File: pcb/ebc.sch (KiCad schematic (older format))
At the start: 43 parts, among them P1 HE10-10, SW1 Switch_SPDT_x2, SW10 SW_PUSH, SW2 SW_PUSH, SW3 SW_PUSH, SW4 SW_PUSH, SW5 SW_PUSH, SW6 SW_PUSH, SW7 SW_PUSH, SW8 SW_PUSH, SW9 SW_PUSH, U1 M24SR64-Y, U2 MSP432P401R, X1 XC9142

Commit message: - schematic almost finished. just trying to pass electrical check
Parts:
- added C15, C18, C19: 10u, symbol C_Small
- added C16, C17: 1u, symbol C_Small
- added D3, D4: RED, symbol LED
- added D5, D6: 1N4148, symbol D_Small
- added P2: CONN_01X30, symbol CONN_01X30
- added R10, R9: 68, symbol R
- added R11: 50, symbol R_Small
- added R12: 600k, symbol R_Small
- D1: value LED -> RED
- gave numbers to parts that had none: 10
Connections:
- net +3V3: now also C18.1, C19.1, P2.17 (P17), P2.18 (P18), P2.27 (P27), P2.4 (P4)
- net 13V: now also C15.1, P2.2 (P2)
- net GND: now also C15.2, C16.2, C17.2, C18.2, C19.2, D5.1 (K), P2.1 (P1), P2.28 (P28), P2.30 (P30), R10.1, R12.2, R9.1
- net ~SHDN: now also U2.6 (P1.2/UCA0RXD/UCA0SOM)
- net at U1.2 (AC0): now also U1.3 (AC1)
- net at X1.2 (GND): now also BT1.1, C2.1, L1.1, X1.3 (BAT)
- net D0: now reaches U2.32 (P3.0/PM_UCA2STE)
- net D0: now also P2.14 (P14)
- net D1: now reaches U2.33 (P3.1/PM_UCA2CLK)
- net D1: now also P2.13 (P13)
- net D2: now reaches U2.34 (P3.2/PM_UCA2RXD/PM_UCA2SOMI)
- net D2: now also P2.12 (P12)
- net D3: now reaches U2.35 (P3.3/PM_UCA2TXD/PM_UCA2SIMO)
- net D3: now also P2.11 (P11)
- net D4: now reaches U2.36 (P3.4/PM_UCB2STE)
- net D4: now also P2.10 (P10)
- net D5: now reaches U2.37 (P3.5/PM_UCB2CLK)
- net D5: now also P2.9 (P9)
- net D6: now reaches U2.38 (P3.6/PM_UCB2SIMO/PM_UCB2SDA)
- net D6: now also P2.8 (P8)
- net D7: now reaches U2.39 (P3.7/PM_UCB2SOMI/PM_UCB2SCL)
- net D7: now also P2.7 (P7)
- net STATUS1: now reaches U2.4 (P1.0/UCA0STE)
- net STATUS1: now also D3.2 (A)
- net CS#: now reaches U2.46 (P8.2/TA3.2/A23)
- net CS#: now also P2.19 (P19)
- net D/C#: now reaches U2.47 (P8.3/TA3CLK/A22)
- net D/C#: now also P2.20 (P20)
- net RES#: now reaches U2.48 (P8.4/A21)
- net RES#: now also P2.21 (P21)
- net E/RD#: now reaches U2.49 (P8.5/A20)
- net E/RD#: now also P2.15 (P15)
- net STATUS2: now reaches U2.5 (P1.1/UCA0CL)
- net STATUS2: now also D4.2 (A)
- net R/W#: now reaches U2.50 (P8.6/A19)
- net R/W#: now also P2.16 (P16)
- net SWCLKTCK renamed TCK
- net SWDIOTMS renamed TMS
- new net: P2.22 (P22), R12.1
- new net: C17.1, P2.26 (P26)
- new net: C16.1, P2.3 (P3)
- new net: P2.5 (P5), R11.1
- new net: D5.2 (A), D6.1 (K)
- new net: D6.2 (A), R11.2
- new net: D3.1 (K), R9.2
- new net: D4.1 (K), R10.2
- no-connect marks 1 -> 60
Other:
- note added: "88.9mm x 50.8\n3.5in x 2in"
- note added: "NC(GND)\nVCC\nVCOMH\nVDDIO\nVSL\nNC\nD7\nD6\nD5\nD4\nD3\nD2\nD1/SDIN\nD0/SCK\nE/RD#\nR/W#\nBS0\nBS1\nCS#\nD/C#\nRES#\nIREF\nGPIO1\nGPIO0\nNC\nVDD\nVCI\nVSS\nNC\nNC(GND)"
- note added: "Rref=(VCC-6V)/IREF\nRref=(13-6)/12.5u\nRref=600k"
- moved on the sheet: C10, C12, C13, C14, D2, L2, R3, R7, R8, SW10, SW2, SW3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

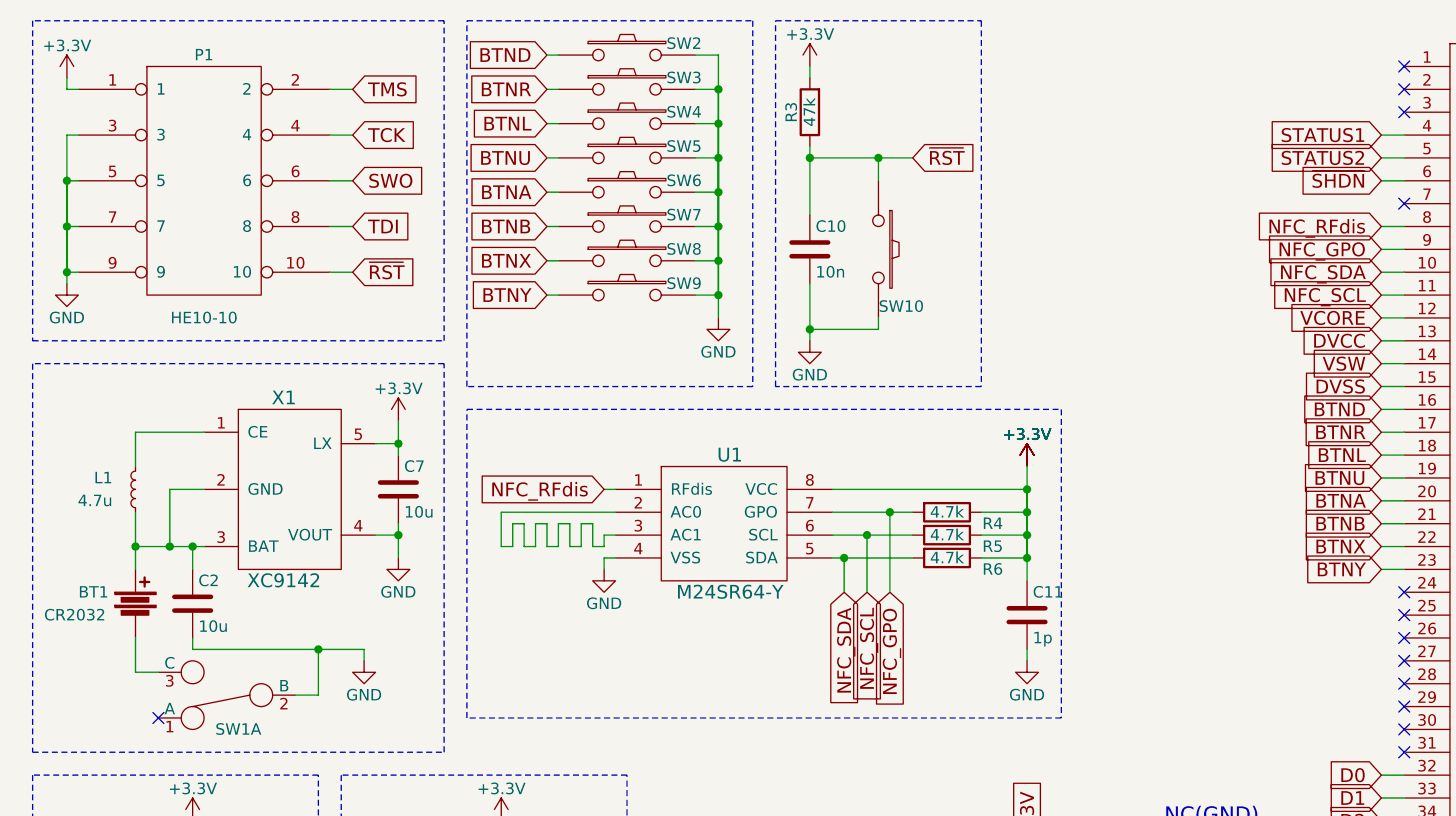
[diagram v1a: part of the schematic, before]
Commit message: - netlist generated, component selection begun
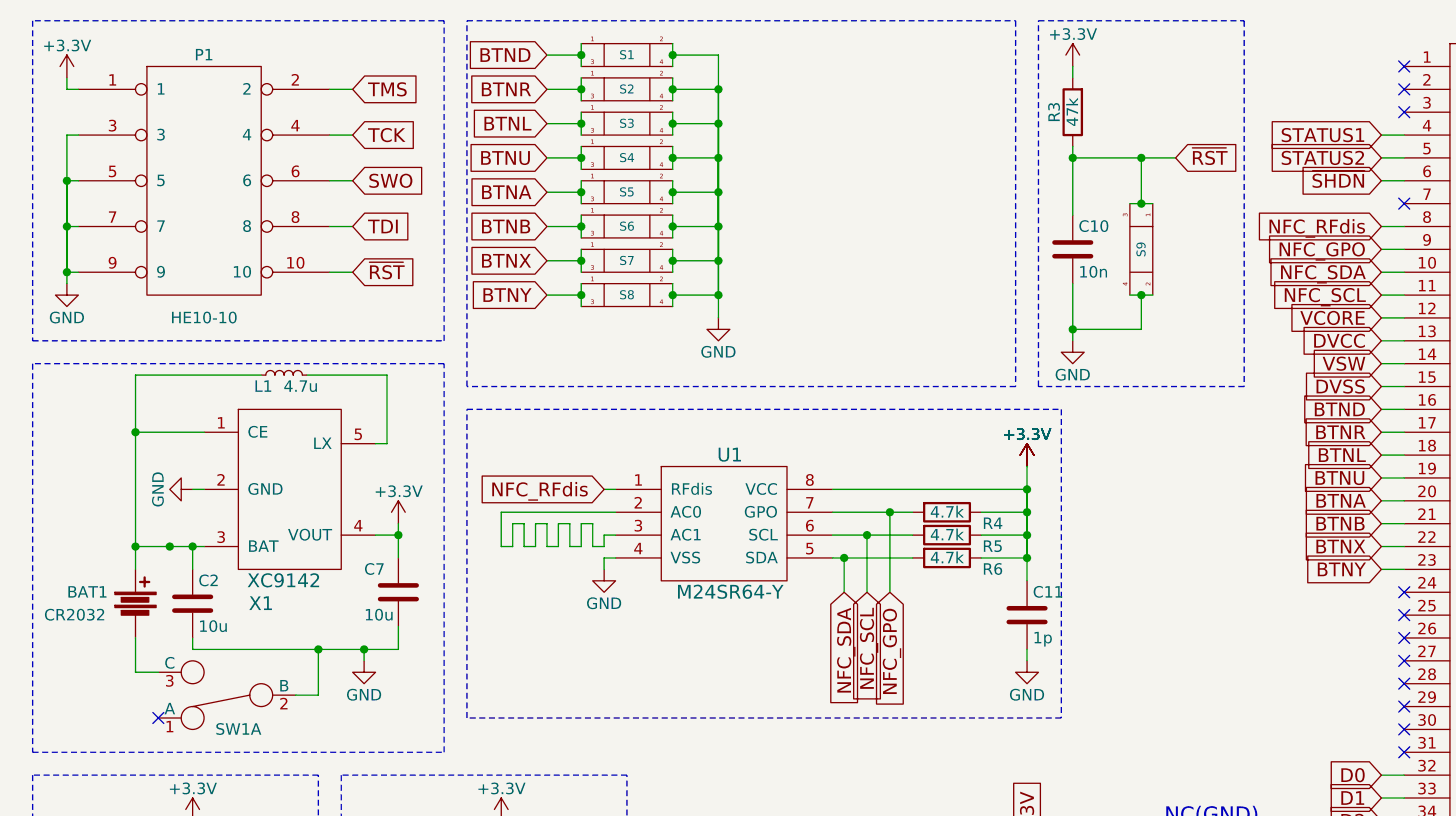
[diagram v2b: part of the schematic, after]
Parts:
- removed SW10, SW2, SW3, SW4, SW5, SW6, SW7, SW8, SW9: SW_PUSH, symbol SW_PUSH
- added S1, S2, S3, S4, S5, S6, S7, S8, S9: 222AMVBAR, rorycad:222AMVBAR, symbol 222AMVBAR
- BAT1: renamed from BT1; footprint (none) -> rorycad:BK-912-G-TR
- U1: footprint (none) -> rorycad:M24SR64-Y
- U2: footprint (none) -> rorycad:MSP432P401R
- U3: footprint (none) -> rorycad:FAN5331
- X1: footprint (none) -> rorycad:XC9142
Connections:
- net +3V3: now also X1.4 (VOUT); no longer X1.5 (LX)
- net BTNA: now also S5.1, S5.3
- net BTNB: now also S6.1, S6.3
- net BTND: now also S1.1, S1.3
- net BTNL: now also S3.1, S3.3
- net BTNR: now also S2.1, S2.3
- net BTNU: now also S4.1, S4.3
- net BTNX: now also S7.1, S7.3
- net BTNY: now also S8.1, S8.3
- net GND: now also X1.2 (GND), S1.2, S1.4, S2.2, S2.4, S3.2, S3.4, S4.2, S4.4, S5.2, S5.4, S6.2, S6.4, S7.2, S7.4, S8.2, S8.4, S9.2, S9.4; no longer X1.4 (VOUT)
- net ~RST: now also S9.1, S9.3
- net at X1.1 (CE): now also BAT1.1, C2.1, L1.1, X1.3 (BAT); no longer L1.2
- new net: L1.2, X1.5 (LX)
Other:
- moved on the sheet: C10, C7, L1, R3

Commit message: - layout about 40% done
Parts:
- removed D2: BAT54, symbol D_Schottky_Small
- added C1: 1n, digikey-footprints:0805, symbol C
- added D3: B130-13-F, digikey-footprints:DO-214AC, symbol D_Schottky
- C10, C11, C12, C13, C14, C15, C16, C17, C18, C19, C2, C3, C4, C5, C6, C7, C8, C9, R1, R10, R11, R12, R2, R7, R8, R9: footprint (none) -> digikey-footprints:0805
- CP1: renamed from C1; footprint (none) -> digikey-footprints:1206
- D1: renamed from D5; footprint (none) -> digikey-footprints:SOD-323
- D2: renamed from D6; footprint (none) -> digikey-footprints:SOD-323
- L1, L2, L3: footprint (none) -> digikey-footprints:1210
- LED1: renamed from D1; footprint (none) -> digikey-footprints:1206
- LED2: renamed from D3; footprint (none) -> digikey-footprints:1206
- LED3: renamed from D4; footprint (none) -> digikey-footprints:1206
- P1: footprint (none) -> rorycad:2x5_PIN_THROUGHHOLE
- P2: footprint (none) -> rorycad:XF2M-3015-1A
- R3: value 47k -> 100k; footprint (none) -> digikey-footprints:0805
- R4, R5, R6: value 4.7k -> 4.3k; footprint (none) -> digikey-footprints:0805
- SW1: footprint (none) -> rorycad:PCM12SMTR
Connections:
- net 13V: now also D3.1 (K)
- net BTNA: now also U2.23 (P2.7/PM_TA0.4); no longer U2.20 (P2.4/PM_TA0.1)
- net BTNB: now also U2.22 (P2.6/PM_TA0.3); no longer U2.21 (P2.5/PM_TA0.2)
- net BTND: now also U2.19 (P2.3/PM_UCA1TXD/PM_UCA1SIMO); no longer U2.16 (P2.0/PM_UCA1STE)
- net BTNU: now also U2.16 (P2.0/PM_UCA1STE); no longer U2.19 (P2.3/PM_UCA1TXD/PM_UCA1SIMO)
- net BTNX: now also U2.21 (P2.5/PM_TA0.2); no longer U2.22 (P2.6/PM_TA0.3)
- net BTNY: now also U2.20 (P2.4/PM_TA0.1); no longer U2.23 (P2.7/PM_TA0.4)
- net CS#: now also U2.48 (P8.4/A21); no longer U2.46 (P8.2/TA3.2/A23)
- net D/C#: now also U2.49 (P8.5/A20); no longer U2.47 (P8.3/TA3CLK/A22)
- net D0: now also U2.39 (P3.7/PM_UCB2SOMI/PM_UCB2SCL); no longer U2.32 (P3.0/PM_UCA2STE)
- net D1: now also U2.38 (P3.6/PM_UCB2SIMO/PM_UCB2SDA); no longer U2.33 (P3.1/PM_UCA2CLK)
- net D2: now also U2.37 (P3.5/PM_UCB2CLK); no longer U2.34 (P3.2/PM_UCA2RXD/PM_UCA2SOMI)
- net D3: now also U2.36 (P3.4/PM_UCB2STE); no longer U2.35 (P3.3/PM_UCA2TXD/PM_UCA2SIMO)
- net D4: now also U2.35 (P3.3/PM_UCA2TXD/PM_UCA2SIMO); no longer U2.36 (P3.4/PM_UCB2STE)
- net D5: now also U2.34 (P3.2/PM_UCA2RXD/PM_UCA2SOMI); no longer U2.37 (P3.5/PM_UCB2CLK)
- net D6: now also U2.33 (P3.1/PM_UCA2CLK); no longer U2.38 (P3.6/PM_UCB2SIMO/PM_UCB2SDA)
- net D7: now also U2.32 (P3.0/PM_UCA2STE); no longer U2.39 (P3.7/PM_UCB2SOMI/PM_UCB2SCL)
- net E/RD#: now also U2.46 (P8.2/TA3.2/A23); no longer U2.49 (P8.5/A20)
- net R/W#: now also U2.47 (P8.3/TA3CLK/A22); no longer U2.50 (P8.6/A19)
- net RES#: now also U2.50 (P8.6/A19); no longer U2.48 (P8.4/A21)
- net D2NEG_TO_D1POS: now reaches D1.2 (A), D2.1 (K)
- net R11NEG_TO_D2POS: now reaches D2.2 (A), R11.2
- net at U1.2 (AC0), U1.3 (AC1): now also C1.1, C1.2
- net SW: now reaches L2.2, U3.1 (SW)
- net SW: now also D3.2 (A)
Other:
- moved on the sheet: C10, C8, C9, LED2, LED3, R10, R3, R9, S9

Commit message: - pcb finished! - unignored gitignore files
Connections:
- net D2NEG_TO_D1POS renamed DIODENET
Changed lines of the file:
@@
 	4900 3400 4800 3400
 Text Label 4100 4850 3    60   ~ 0
-D2NEG_TO_D1POS
+DIODENET
 Wire Wire Line
 	4100 4650 4100 4850
